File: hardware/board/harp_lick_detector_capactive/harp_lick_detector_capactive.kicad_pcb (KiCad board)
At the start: 4 copper layers, 80 x 50 mm, 145 parts, among them J2 Conn_01x03_Male, J3 Conn_Triaxial, J4 AudioJack3, J5 USB_C_Receptacle_USB2.0, J6 Barrel_Jack_Switch, J7 Conn_Coaxial, U1 74LVCH2T45DC, U11 LM27762, U12 LT3030, U13 ADS7049, U2 TPD2EUSB30, U3 ADUM4160, U4 RP2040, U5 W25Q16JVUXIQ, U6 LTC6263, U7 LTC6268xS8-10, U8 REF2033, X1 ECS-TXO-2016

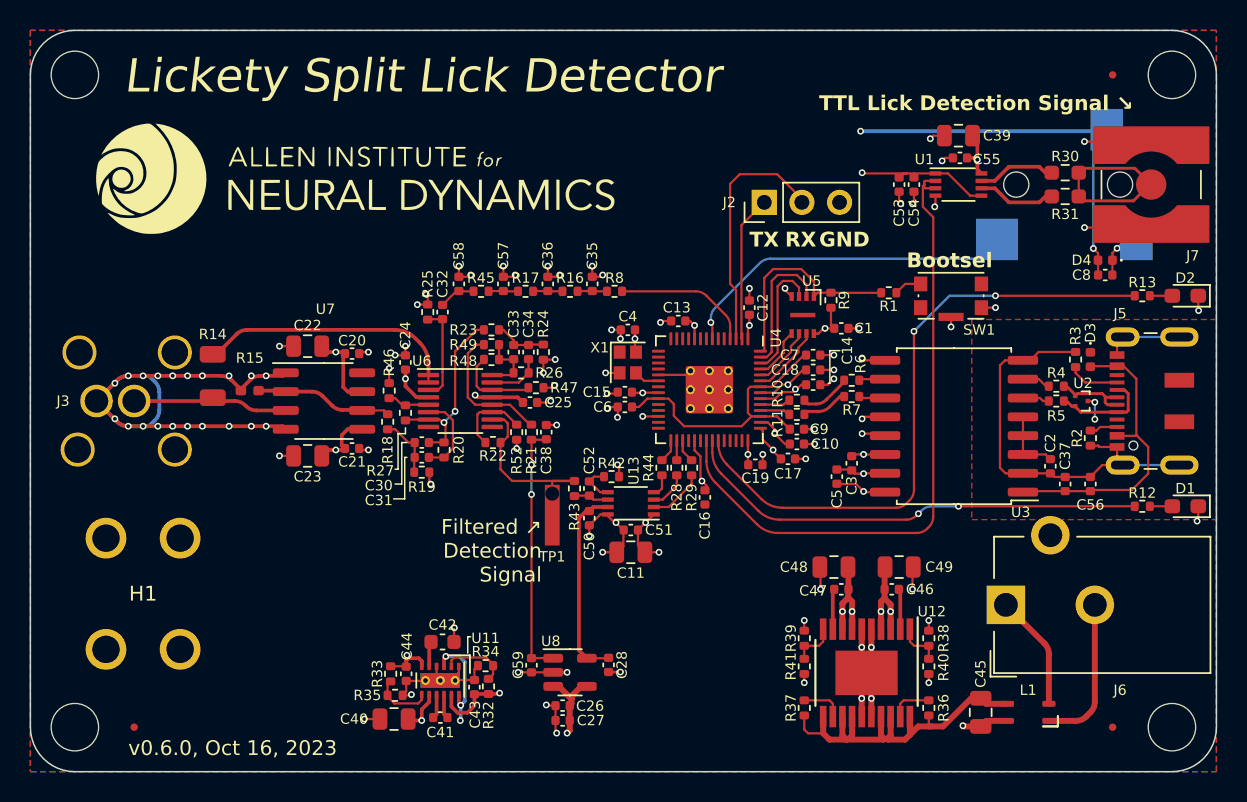
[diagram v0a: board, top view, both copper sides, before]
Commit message: update layout for v0.6.1
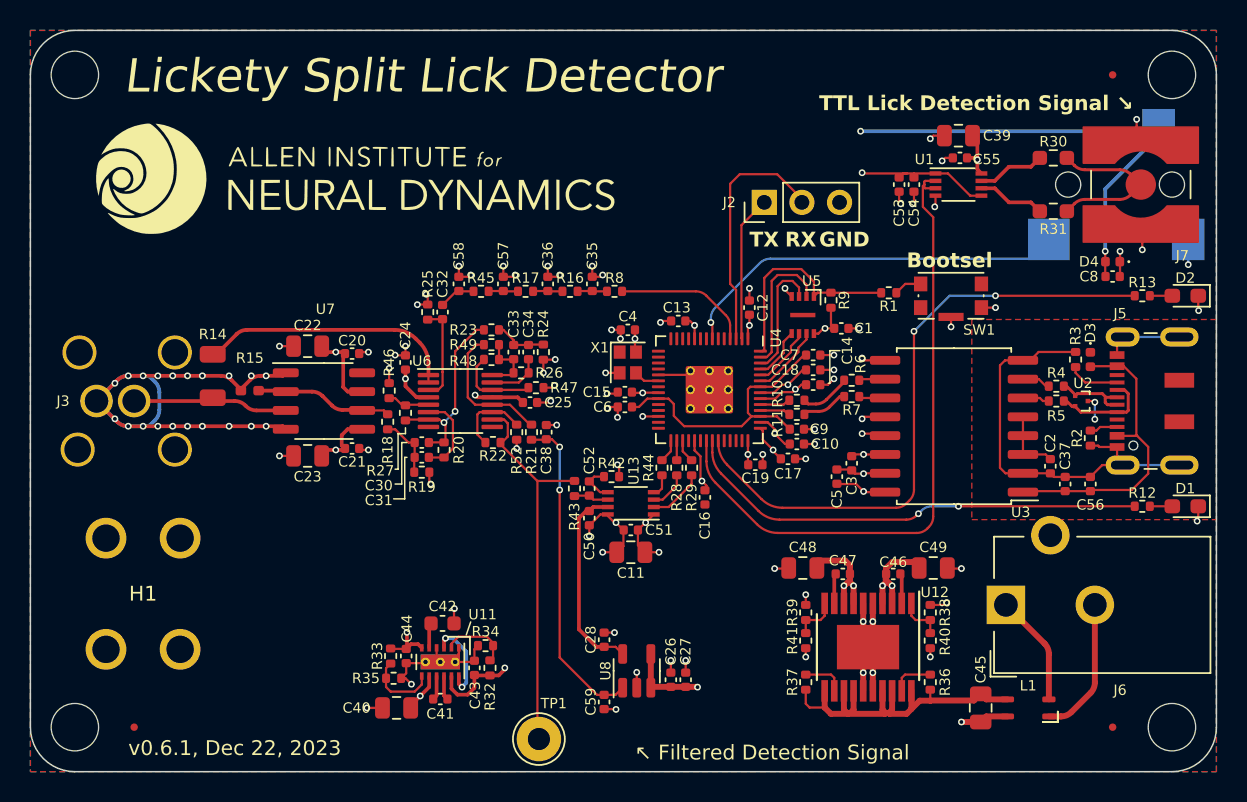
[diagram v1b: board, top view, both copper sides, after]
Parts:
- R42, R43: value 68 -> 127
- TP1: footprint kicad_component_library:TestPoint_Keystone_5027_Miniature -> TestPoint:TestPoint_THTPad_D3.0mm_Drill1.5mm
- U8: value REF2033 -> REF2025
- moved TP1 15.1 mm to (139.2, 115.8)
- moved C27 8.74 mm to (149.1, 111.8), turned to 90 degrees
- moved C26 7.51 mm to (148.1, 111.8), turned to -90 degrees
- moved C59 5.49 mm to (143.6, 113.3)
- moved U8 4.50 mm to (145.8, 111.2), turned to 90 degrees
- moved J4 3.50 mm to (179.4, 78.4)
- moved G1 3.10 mm to (122.4, 79.7)
- moved C49 2.30 mm to (165.8, 104.3)
- moved C48 2.10 mm to (157.0, 104.3)
- moved R40 1.74 mm to (165.6, 109.2)
- moved R41 1.74 mm to (157.2, 109.2)
- moved U12 1.74 mm to (161.4, 109.6)
- moved R36 1.74 mm to (165.6, 112.0)
- moved R37 1.74 mm to (157.2, 112.0)
- moved R38 1.74 mm to (165.6, 107.3)
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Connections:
- net VREF_1V65 renamed VREF_1V25
- net VREF_3V3 renamed VREF_2V5
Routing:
- net Net-(R22-Pad1): track 12.2 -> 26.3 mm
- net GND: track 107.3 -> 99.3 mm, vias 76 -> 77
- net +3V3: track 85.4 -> 90.9 mm
- net VREF_1V25: track 17.2 -> 21.8 mm
- net /Harp Core RP2040 + Isolated USB/HARP_CLK_SYNC: track 23.1 -> 26.6 mm
- net Net-(J7-In): track 12.5 -> 11.3 mm
- net Net-(U11-FB-): track 4.07 -> 5.02 mm
- net GND2: track 10.3 -> 9.43 mm
- net +2V5: track 13.7 -> 14.4 mm
- net Net-(U12-BYP2): track 2.73 -> 2.03 mm
- net Net-(U12-BYP1): track 2.73 -> 2.03 mm
- net IN1: track 26.0 -> 25.3 mm
- net +5V: track 26.3 -> 26.2 mm, vias 9 -> 8
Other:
- board text added: "Source Files & Setup →"
- board text added: "v0.6.1, Dec 22, 2023"
- board text added: "↖ Filtered Detection Signal"
- board text removed: "Filtered ↗ Detection Signal"
- board text removed: "Fits in enclosure: 1457C801E or 1457C801EBK"
- board text removed: "Source Files & Setup ↓"
- board text removed: "v0.6.0, Oct 16, 2023"

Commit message: update lickety split 0.6.1 pcb files
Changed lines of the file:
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@@
       (drillshape 0)
       (scaleselection 1)
-      (outputdirectory "exports/lickety_split_r0.6/gerbers/")
+      (outputdirectory "exports/lickety_split_r0.6.1/gerbers/")
     )
   )
@@
     (effects (font (size 1 1) (thickness 0.2) bold) (justify left bottom))
   )
+  (gr_text "Sonya Vasquez" (at 166.8 117) (layer "F.SilkS")
+    (effects (font (size 1 1) (thickness 0.15)) (justify left bottom))
+  )
   (gr_text "TTL Lick Detection Signal ↘" (at 158.1 73.5) (layer "F.SilkS")
     (effects (font (size 1 1) (thickness 0.2) bold) (justify left bottom))
@@
     (effects (font (size 1 1) (thickness 0.2) bold) (justify left bottom))
   )
-  (gr_text "Sonya Vasquez" (at 166.8 117) (layer "F.Mask")
-    (effects (font (size 1 1) (thickness 0.15)) (justify left bottom))
-  )
   (segment (start 166.7875 104.3) (end 166.75 104.2625) (width 0.1524) (layer "F.Cu") (net 1))

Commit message: hotfix v0.6.1 pcb triax connector footprint
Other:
- board text added: "v0.6.1, Jan 10, 2024"
- board text removed: "v0.6.1, Dec 22, 2023"
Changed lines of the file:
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@@
     (pad "3" thru_hole circle (at -3.2766 2.7432 90) (size 2.3 2.3) (drill 1.8) (layers "*.Cu" "*.Mask")
       (net 1 "GND") (pinfunction "Shield") (pintype "passive"))
-    (pad "3" thru_hole circle (at 3.2766 -3.69 90) (size 2.3 2.3) (drill 1.8) (layers "*.Cu" "*.Mask")
+    (pad "3" thru_hole circle (at 3.2766 -3.81 90) (size 2.3 2.3) (drill 1.8) (layers "*.Cu" "*.Mask")
       (net 1 "GND") (pinfunction "Shield") (pintype "passive"))
     (pad "3" thru_hole circle (at 3.2766 2.7432 90) (size 2.3 2.3) (drill 1.8) (layers "*.Cu" "*.Mask")
       (net 1 "GND") (pinfunction "Shield") (pintype "passive"))
-    (model "/home/poofjunior/projects/kicad_libraries/kicad_component_library/kicad_component_library.3dshapes/CBBJR79A.step"
-      (offset (xyz 0 0.5 0))
-      (scale (xyz 1 1 1))
-      (rotate (xyz 90 180 -90))
-    )
   )
   (footprint "Resistor_SMD:R_0402_1005Metric" (layer "F.Cu")
@@
     (effects (font (size 2.25 2.25) (thickness 0.4) italic) (justify left bottom))
   )
-  (gr_text "v0.6.1, Dec 22, 2023" (at 111.5 117) (layer "F.SilkS")
+  (gr_text "v0.6.1, Jan 10, 2024" (at 111.5 117) (layer "F.SilkS")
     (effects (font (size 1 1) (thickness 0.15)) (justify left bottom))
   )

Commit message: draft v0.7 pcb schematic and layout
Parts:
- added C29: 100nF, Capacitor_SMD:C_0402_1005Metric, F.Cu at (139.0, 91.6)
- added C60: 100nF, Capacitor_SMD:C_0402_1005Metric, F.Cu at (137.3, 99.2)
- added C61: 100nF, Capacitor_SMD:C_0402_1005Metric, F.Cu at (133.5, 81.7)
- added C62: 100nF, Capacitor_SMD:C_0402_1005Metric, F.Cu at (136.3, 84.6)
- added C63: 100nF, Capacitor_SMD:C_0402_1005Metric, F.Cu at (129.3, 81.1)
- added C64: 100nF, Capacitor_SMD:C_0402_1005Metric, F.Cu at (141.1, 99.2)
- added C65: 100nF, Capacitor_SMD:C_0402_1005Metric, F.Cu at (138.6, 105.9)
- added C66: 100nF, Capacitor_SMD:C_0402_1005Metric, F.Cu at (141.2, 103.0)
- added R50: 2K2, Resistor_SMD:R_0402_1005Metric, F.Cu at (147.2, 83.6)
- added R51: 100K, Resistor_SMD:R_0402_1005Metric, F.Cu at (135.9, 94.5)
- added R53: 100K, Resistor_SMD:R_0402_1005Metric, F.Cu at (139.7, 94.5)
- added R54: 1K00, Resistor_SMD:R_0402_1005Metric, F.Cu at (130.0, 82.5)
- added R55: 100K, Resistor_SMD:R_0402_1005Metric, F.Cu at (131.4, 83.0)
- added R56: 1K00, Resistor_SMD:R_0402_1005Metric, F.Cu at (132.4, 83.0)
- added U14: TS5A9411DCKR, Package_TO_SOT_SMD:SOT-363_SC-70-6, F.Cu at (136.9, 92.0)
- added U15: LTC6081xMS8, Package_SO:MSOP-8_3x3mm_P0.65mm, F.Cu at (133.5, 92.0)
- added U16: AD8615, Package_TO_SOT_SMD:TSOT-23-5, F.Cu at (138.6, 103.5)
- added U17: AD8615, Package_TO_SOT_SMD:TSOT-23-5, F.Cu at (135.7, 82.0)
- added U18: TS5A9411DCKR, Package_TO_SOT_SMD:SOT-363_SC-70-6, F.Cu at (131.4, 80.6)
- added U9: TS5A9411DCKR, Package_TO_SOT_SMD:SOT-363_SC-70-6, F.Cu at (136.8, 97.1)
- C30, C31: value 150pF -> 160pF
- C33, C34: value 160pF -> 130pF
- R18: value 105K -> 200K
- R19, R49, R52: value 1K02 -> 1K00
- R20, R21, R22: value 102K -> 100K
- R23: value 105K -> 249K
- R24: value 1K05 -> 976
- R26: value 102K -> 97K6
- R27: value 9K53 -> 9K76
- R46: value 124 -> 147
- R47: value 127 -> 140
- R48: value 9K76 -> 8K66
- U6: value LTC6263 -> TS5A9411DCKR; footprint Package_SO:MSOP-16_3x4mm_P0.5mm -> Package_TO_SOT_SMD:SOT-363_SC-70-6
- moved C33 10.7 mm to (128.9, 96.1)
- moved R24 10.6 mm to (129.9, 94.2), turned to -90 degrees
- moved R22 10.3 mm to (142.4, 103.9), turned to -90 degrees
- moved R26 9.52 mm to (129.9, 96.1), turned to -90 degrees
- moved C34 9.38 mm to (130.9, 95.2)
- moved R23 9.30 mm to (128.9, 94.2), turned to -90 degrees
- moved R43 9.25 mm to (147.7, 105.8), turned to 180 degrees
- moved R20 8.79 mm to (129.9, 88.0)
- moved R25 8.61 mm to (138.4, 81.6), turned to 0 degrees
- moved R47 8.40 mm to (132.4, 97.3), turned to 0 degrees
- moved C50 8.35 mm to (149.6, 105.5), turned to 180 degrees
- moved C30 8.16 mm to (128.9, 88.0), turned to 90 degrees
- moved R19 8.02 mm to (129.9, 89.9), turned to 90 degrees
- moved U6 7.94 mm to (140.7, 97.1), turned to 90 degrees
- moved C52 7.84 mm to (147.7, 104.8), turned to 180 degrees
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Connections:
- net /100KHz Sine Wave/100KHZ_SQ_WAVE_IN renamed /100KHz Sine Wave/100KHZ_IN
- C31 pad 2: Net-(U6B--) -> Net-(U15B--)
- C32 pad 2: Net-(U6A-+) -> Net-(U17-+)
- C34 pad 2: Net-(U6D--) -> Net-(U15A--)
- R20 pad 1: Net-(U6B--) -> Net-(U15B--)
- R21 pad 1: Net-(U6C-+) -> VREF_1V25
- R21 pad 2: VREF_1V25 -> Net-(U16-+)
- R22 pad 1: Net-(R22-Pad1) -> Net-(U16--)
- R22 pad 2: Net-(U6C--) -> Net-(R22-Pad2)
- R23 pad 1: Net-(C30-Pad2) -> Net-(U7--)
- R25 pad 1: Net-(U6A-+) -> Net-(U17-+)
- R26 pad 1: Net-(U6D--) -> Net-(U15A--)
- R27 pad 1: Net-(U6B-+) -> Net-(U15B-+)
- R43 pad 2: Net-(R22-Pad1) -> Net-(R22-Pad2)
- R46 pad 2: Net-(U6B-+) -> Net-(U15B-+)
- R47 pad 2: Net-(U6D-+) -> Net-(U15A-+)
- R48 pad 1: Net-(U6D-+) -> Net-(U15A-+)
- R49 pad 1: Net-(U6C-+) -> Net-(R49-Pad1)
- R49 pad 2: Net-(C33-Pad2) -> Net-(R49-Pad2)
- R52 pad 1: Net-(U6C--) -> Net-(R52-Pad1)
- TP1 pad 1: Net-(R22-Pad1) -> Net-(R22-Pad2)
- U4 pad 27: unconnected-(U4-GPIO16-Pad27) -> FILTER_SEL
- U4 pad 28: unconnected-(U4-GPIO17-Pad28) -> GAIN_SEL
- U4 pad 5: unconnected-(U4-GPIO3-Pad5) -> /100KHz Sine Wave/125KHZ_IN
- U6 pad 1: /100KHz Sine Wave/VSINE -> GAIN_SEL
- U6 pad 2: /100KHz Sine Wave/VSINE -> +3V3
- U6 pad 3: Net-(U6A-+) -> GND
- U6 pad 4: +2V5 -> Net-(R52-Pad1)
- U6 pad 5: Net-(U6B-+) -> Net-(U16--)
- U6 pad 6: Net-(U6B--) -> Net-(R53-Pad1)
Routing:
- net GAIN_SEL: track 0.00 -> 48.6 mm, vias 0 -> 5
- net +3V3: track 90.9 -> 120.5 mm, vias 24 -> 28
- net Net-(R22-Pad1): track 26.3 -> 0.00 mm
- net Net-(R22-Pad2): track 0.00 -> 20.6 mm
- net -2V5: track 11.2 -> 29.7 mm, vias 3 -> 5
- net Net-(U16--): track 0.00 -> 14.8 mm
- net FILTER_SEL: track 0.00 -> 10.2 mm
- net Net-(U16-+): track 0.00 -> 9.99 mm, vias 0 -> 2
- net Net-(U6C-+): track 9.35 -> 0.00 mm
- net GND: track 99.3 -> 106.8 mm
- net /100KHz Sine Wave/125KHZ_IN: track 0.00 -> 7.10 mm
- net Net-(U6A-+): track 6.56 -> 0.00 mm
- net Net-(C33-Pad2): track 4.42 -> 10.2 mm
- net Net-(U6B--): track 5.66 -> 0.00 mm
- net Net-(U6D-+): track 5.66 -> 0.00 mm
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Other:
- board text added: "v0.7.0, April 4, 2024"
- board text removed: "v0.6.1, Jan 10, 2024"

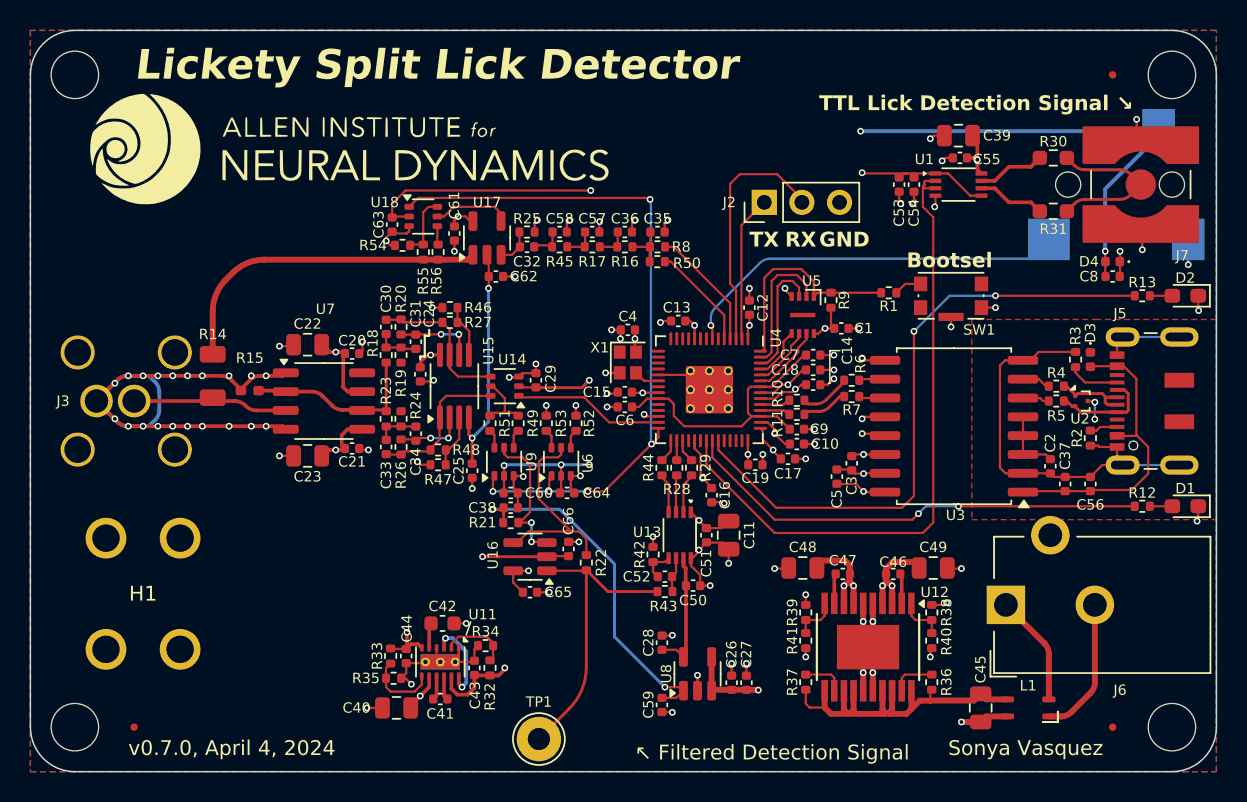
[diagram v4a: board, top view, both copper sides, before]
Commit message: implement soe feedback in layout
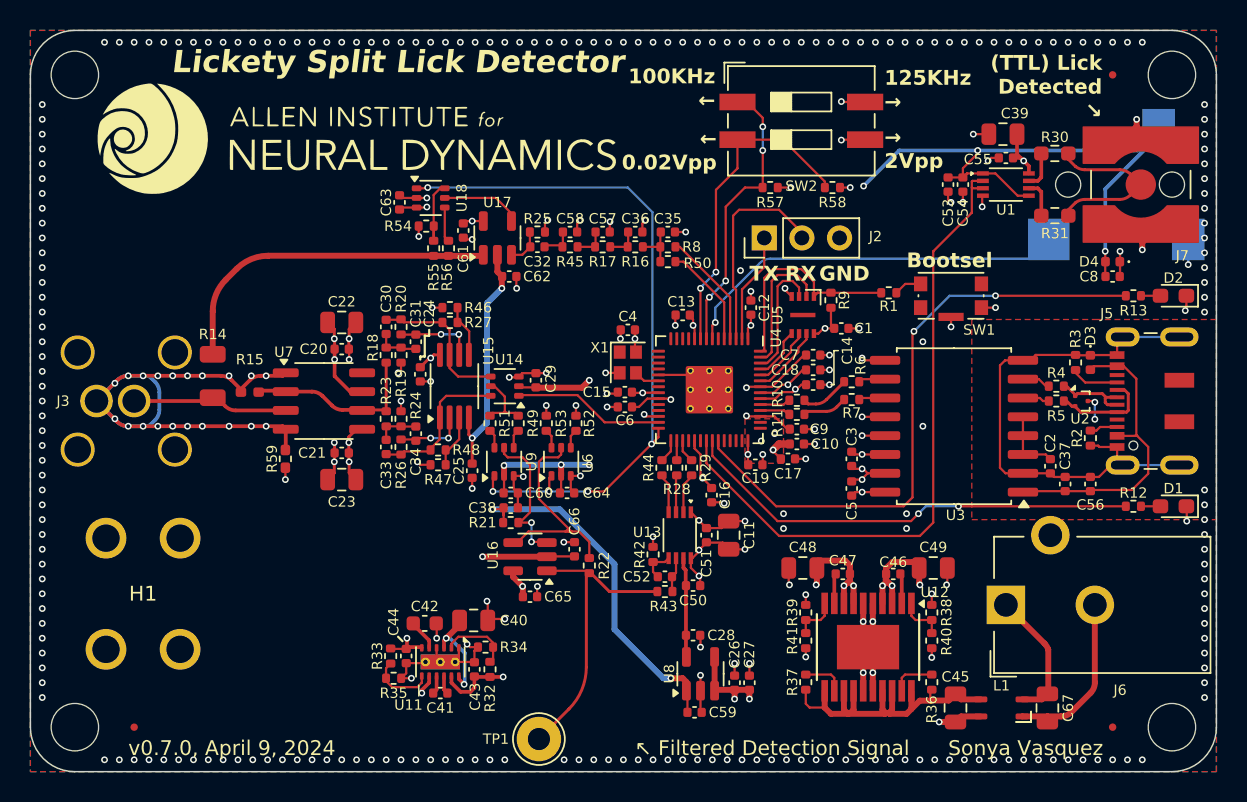
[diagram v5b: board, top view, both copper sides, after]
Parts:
- added C67: 3.3uF, Capacitor_SMD:C_0805_2012Metric, F.Cu at (173.5, 113.7)
- added R57: 10K, Resistor_SMD:R_0402_1005Metric, F.Cu at (154.8, 78.6)
- added R58: 10K, Resistor_SMD:R_0402_1005Metric, F.Cu at (159.0, 78.6)
- added R59: 0, Resistor_SMD:R_0402_1005Metric_Pad0.72x0.64mm_HandSolder, F.Cu at (122.1, 96.9)
- added SW2: SW_DIP_x02, Button_Switch_SMD:SW_DIP_SPSTx02_Slide_9.78x7.26mm_W8.61mm_P2.54mm, F.Cu at (156.9, 74.1)
- moved C40 7.86 mm to (134.8, 107.8), turned to 0 degrees
- moved C53 3.30 mm to (166.8, 78.4)
- moved C54 3.30 mm to (167.8, 78.4)
- moved U1 3.20 mm to (170.7, 78.4)
- moved C55 3.10 mm to (170.7, 76.6)
- moved C39 3.00 mm to (170.5, 75.0)
- moved C23 2.80 mm to (125.9, 98.3)
- moved C22 2.75 mm to (125.9, 87.7), turned to 180 degrees
- moved J2 2.40 mm to (154.4, 82.0)
- moved C59 2.26 mm to (149.7, 114.0), turned to 180 degrees
- moved C28 2.16 mm to (149.6, 108.8), turned to 180 degrees
- moved R54 2.06 mm to (131.6, 81.2)
- moved L1 1.80 mm to (170.4, 113.7)
- moved C45 1.70 mm to (167.3, 113.7)
- moved C63 1.58 mm to (129.8, 79.6)
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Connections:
- U4 pad 8: unconnected-(U4-GPIO6-Pad8) -> /Harp Core RP2040 + Isolated USB/FREQ_SEL_DIP
- U4 pad 9: unconnected-(U4-GPIO7-Pad9) -> /Harp Core RP2040 + Isolated USB/GAIN_SEL_DIP
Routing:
- net /Harp Core RP2040 + Isolated USB/GAIN_SEL_DIP: track 0.00 -> 21.9 mm, vias 0 -> 2
- net /Harp Core RP2040 + Isolated USB/FREQ_SEL_DIP: track 0.00 -> 19.3 mm, vias 0 -> 4
- net +3V3: track 120.5 -> 106.2 mm, vias 28 -> 33
- net +1V1: track 19.6 -> 11.1 mm, vias 0 -> 3
- net GND: track 106.8 -> 114.6 mm, vias 77 -> 299
- net GND1: track 35.6 -> 38.2 mm, vias 2 -> 4
- net /Harp Core RP2040 + Isolated USB/UART0_RXD: track 16.6 -> 14.2 mm
- net /Harp Core RP2040 + Isolated USB/UART0_TXD: track 9.85 -> 7.42 mm
- net GND2: track 9.43 -> 11.6 mm
- net Net-(U1-2B): track 4.58 -> 2.55 mm
- net Net-(U1-1B): track 4.58 -> 2.55 mm
- net IN1: track 25.4 -> 23.6 mm
- net VREF_2V5: track 8.45 -> 6.75 mm
- net +2V5: track 18.0 -> 16.3 mm, vias 5 -> 6
- net /Lick Detection Analog Front End/triax_inner_shield: track 40.1 -> 41.7 mm
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- added copper zone on In2.Cu, net +1V1
- added copper zone on F.Cu, net +3V3
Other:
- board text added: "(TTL) Lick Detected ↘"
- board text added: "100KHz ←"
- board text added: "125KHz →"
- board text added: "Setup Notes: • The animal must share a ground with this board through the ground lug or barrel jack power plug. • USB and 3.5mm (Harp) connections are not needed if solely using the TTL output."
- board text added: "v0.7.0, April 9, 2024"
- board text added: "← 0.02Vpp"
- board text added: "→ 2Vpp"
- board text removed: "Setup Notes: • The animal must share a ground with this board through the ground lug. • USB and 3.5mm (Harp) connections are not needed if solely using the TTL output."
- board text removed: "TTL Lick Detection Signal ↘"
- board text removed: "v0.7.0, April 4, 2024"
